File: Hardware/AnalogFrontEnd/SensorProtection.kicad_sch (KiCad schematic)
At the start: 0 parts

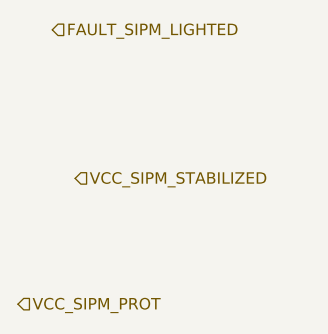
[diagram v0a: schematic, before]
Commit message: add draft of data processing circuit
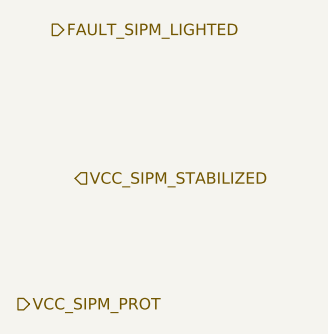
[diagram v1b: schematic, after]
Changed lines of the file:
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@@
 	)
 	(hierarchical_label "VCC_SIPM_PROT"
-		(shape input)
+		(shape output)
 		(at 119.38 123.19 0)
 		(effects
@@
 	)
 	(hierarchical_label "FAULT_SIPM_LIGHTED"
-		(shape input)
+		(shape output)
 		(at 123.19 92.71 0)
 		(effects
